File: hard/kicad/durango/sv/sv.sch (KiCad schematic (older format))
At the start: 27 parts, among them J1 6502 DATA BUS, J2 SVGA, J3 CONTROL, J4 6502 ADDRESS BUS, U1 74HCT02, U10 74HC245, U11 74HCT374, U12 74HC245, U13 74HC257, U14 6264, U15 74HC257, U16 74HC257, U17 74HC257, U18 74HC257, U2 74HCT4040, U3 74HC21, U4 74HCT4040, U5 74HC21, U6 74HCT85, U7 74HCT85, U8 74HCT85, U9 74HC175, X1 ACO-18.432MHz

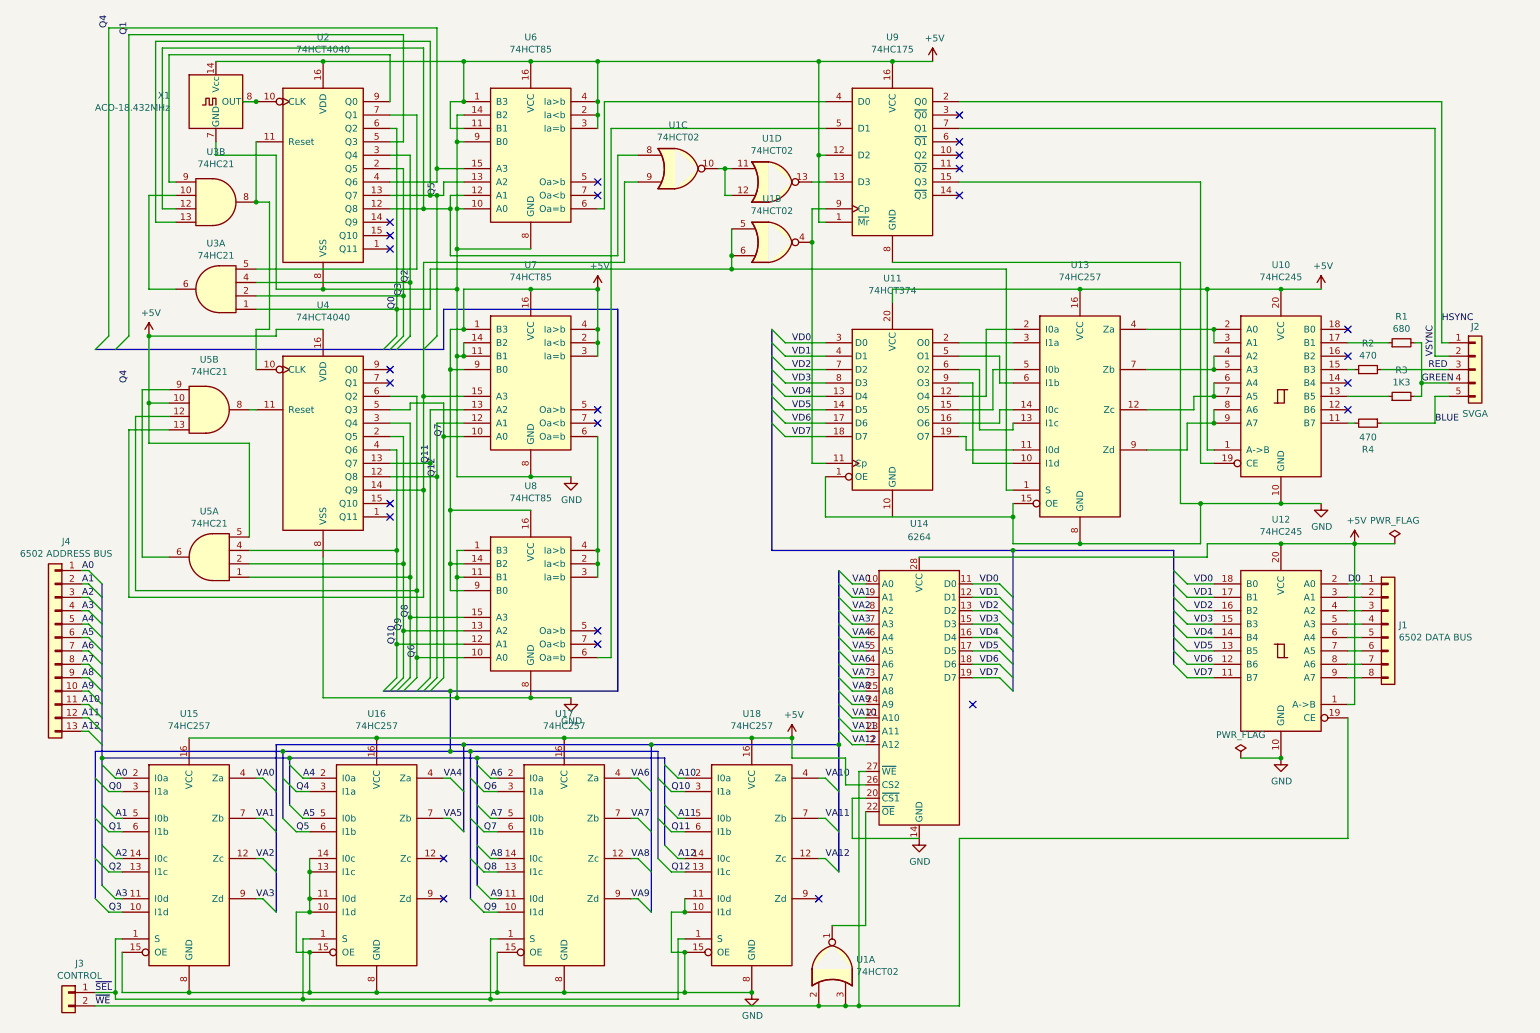
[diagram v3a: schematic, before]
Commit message: line clock from HS on all tree VDUs
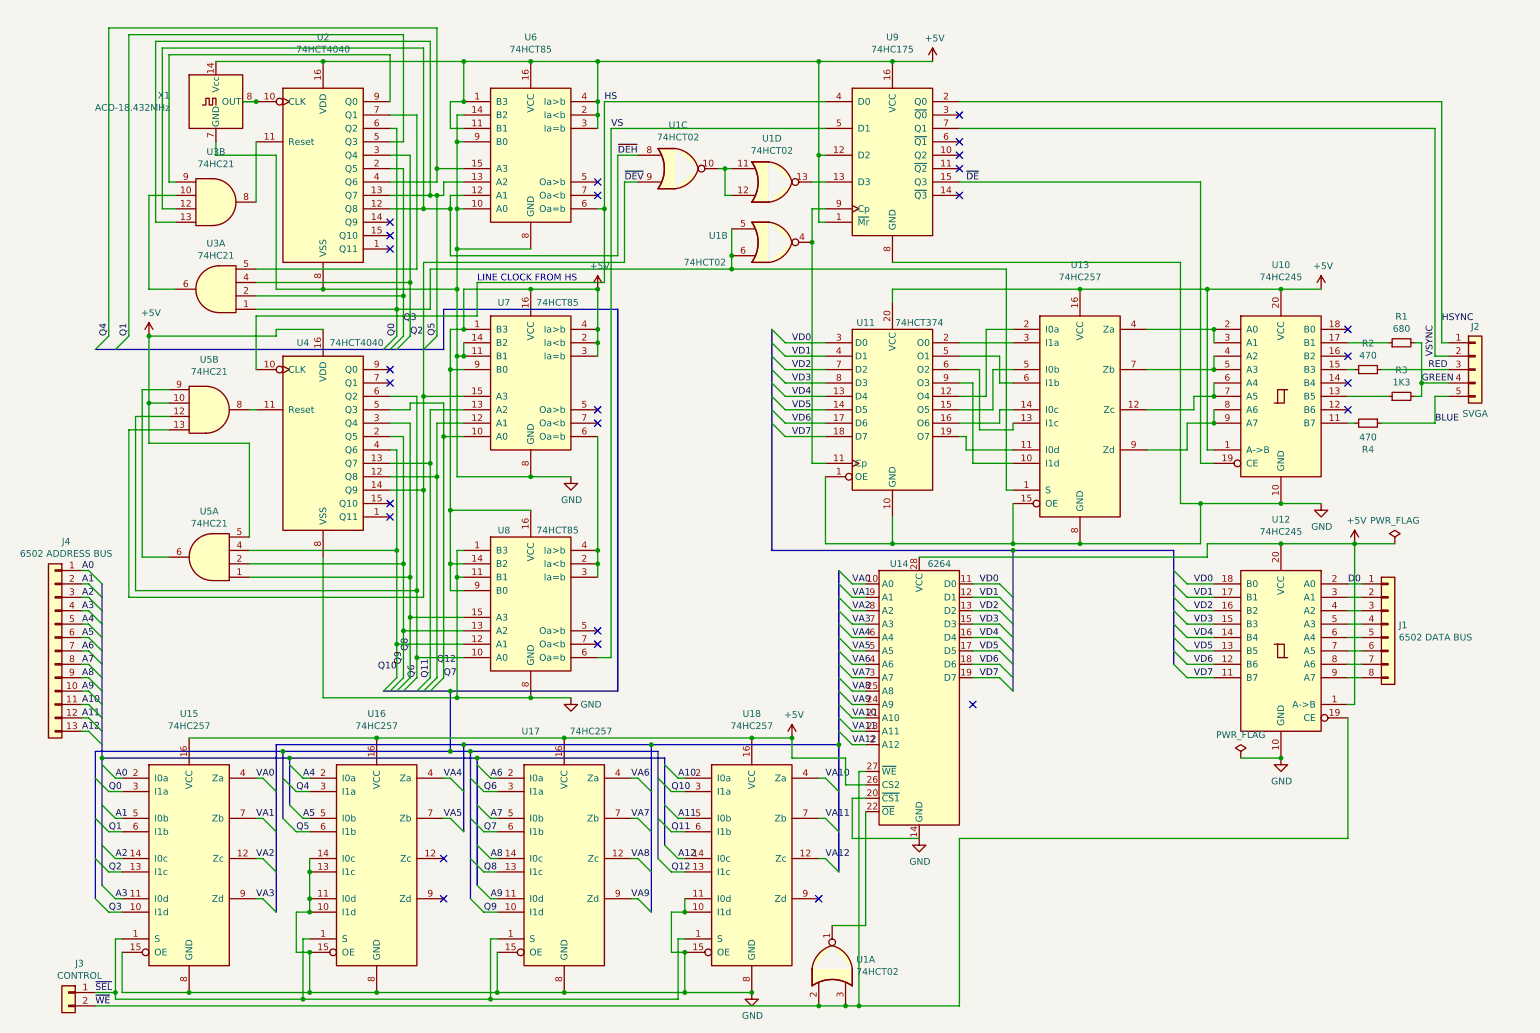
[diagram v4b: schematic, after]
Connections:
- net GND: now also U11.10 (GND)
- net ~DEH: now reaches U1.8, U2.12 (Q8), U3.12, U6.12 (A1)
- net ~DEV: now reaches U1.9, U4.14 (Q9), U5.13, U7.15 (A3)
- net at U2.11 (Reset), U3.8: no longer U4.10 (CLK)
- net HS: now reaches U6.6 (Oa=b), U9.4 (D0)
- net HS: now also U4.10 (CLK)
- net VS: now reaches U8.6 (Oa=b), U9.5 (D1)
- net ~DE: now reaches U10.19 (CE), U9.15 (Q3)
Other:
- note added: "LINE CLOCK FROM HS"
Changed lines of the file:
@@
 EESchema Schematic File Version 4
-LIBS:sv-cache
-EELAYER 29 0
+EELAYER 30 0
 EELAYER END
 $Descr A4 11693 8268
@@
 U 1 1 6066AB07
 P 2400 3500
-F 0 "U4" H 2400 4481 50  0000 C CNN
-F 1 "74HCT4040" H 2400 4390 50  0000 C CNN
+F 0 "U4" H 2250 4200 50  0000 C CNN
+F 1 "74HCT4040" H 2650 4200 50  0000 C CNN
 F 2 "" H 2400 3500 50  0001 C CNN
 F 3 "http://www.intersil.com/content/dam/Intersil/documents/cd40/cd4020bms-24bms-40bms.pdf" H 2400 3500 50  0001 C CNN
@@
 U 1 1 60692E60
 P 3950 3100
-F 0 "U7" H 3950 3981 50  0000 C CNN
-F 1 "74HCT85" H 3950 3890 50  0000 C CNN
+F 0 "U7" H 3750 3700 50  0000 C CNN
+F 1 "74HCT85" H 4150 3700 50  0000 C CNN
 F 2 "" H 3950 3100 50  0001 C CNN
 F 3 "http://www.ti.com/lit/gpn/sn74LS85" H 3950 3100 50  0001 C CNN
@@
 U 1 1 6069676C
 P 3950 4750
-F 0 "U8" H 3950 5631 50  0000 C CNN
-F 1 "74HCT85" H 3950 5540 50  0000 C CNN
+F 0 "U8" H 3750 5300 50  0000 C CNN
+F 1 "74HCT85" H 4150 5300 50  0000 C CNN
 F 2 "" H 3950 4750 50  0001 C CNN
 F 3 "http://www.ti.com/lit/gpn/sn74LS85" H 3950 4750 50  0001 C CNN
@@
 U 1 1 6075F5C4
 P 6650 3300
-F 0 "U11" H 6650 4281 50  0000 C CNN
-F 1 "74HCT374" H 6650 4190 50  0000 C CNN
+F 0 "U11" H 6450 3950 50  0000 C CNN
+F 1 "74HCT374" H 6850 3950 50  0000 C CNN
 F 2 "" H 6650 3300 50  0001 C CNN
 F 3 "https://www.ti.com/lit/ds/symlink/cd74hct374.pdf" H 6650 3300 50  0001 C CNN
@@
 	1050 3150 1250 3150
 Wire Wire Line
-	1900 1750 2000 1750
-Wire Wire Line
-	2000 1750 2000 2700
-Wire Wire Line
-	2000 2700 1900 2700
-Wire Wire Line
-	1900 2700 1900 3000
-Connection ~ 1900 1750
-Wire Wire Line
 	1900 2550 2950 2550
 Wire Wire Line
@@
 Connection ~ 9050 3400
 Wire Wire Line
-	7550 4000 7550 4100
-Wire Wire Line
 	7550 4300 8050 4300
 Wire Wire Line
@@
 U 2 1 60C66774
 P 5750 2050
-F 0 "U1" H 5750 2375 50  0000 C CNN
-F 1 "74HCT02" H 5750 2284 50  0000 C CNN
+F 0 "U1" H 5350 2100 50  0000 C CNN
+F 1 "74HCT02" H 5250 1900 50  0000 C CNN
 F 2 "" H 5750 2050 50  0001 C CNN
 F 3 "http://www.ti.com/lit/gpn/sn7402" H 5750 2050 50  0001 C CNN
@@
 P 4250 5450
 F 0 "#PWR0107" H 4250 5200 50  0001 C CNN
-F 1 "GND" H 4255 5277 50  0000 C CNN
+F 1 "GND" H 4400 5400 50  0000 C CNN
 F 2 "" H 4250 5450 50  0001 C CNN
 F 3 "" H 4250 5450 50  0001 C CNN
@@
 	1600 1400 1600 1300
 Connection ~ 2400 2400
-Connection ~ 7550 4100
-Wire Wire Line
-	7550 4100 7550 4300
 Wire Wire Line
 	8050 4300 8950 4300
@@
 U 1 1 606818EE
 P 6850 5400
-F 0 "U14" H 6850 6650 50  0000 C CNN
-F 1 "6264" H 6850 6550 50  0000 C CNN
+F 0 "U14" H 6700 6350 50  0000 C CNN
+F 1 "6264" H 7000 6350 50  0000 C CNN
 F 2 "Package_DIP:DIP-28_W15.24mm" H 6850 5400 50  0001 C CNN
 F 3 "http://users.ece.utexas.edu/~valvano/Datasheets/MCM6264.pdf" H 6850 5400 50  0001 C CNN
@@
 U 1 1 608343C4
 P 4200 6650
-F 0 "U17" H 4200 7731 50  0000 C CNN
-F 1 "74HC257" H 4200 7640 50  0000 C CNN
+F 0 "U17" H 3950 7600 50  0000 C CNN
+F 1 "74HC257" H 4400 7600 50  0000 C CNN
 F 2 "" H 4200 6650 50  0001 C CNN
 F 3 "http://www.ti.com/lit/gpn/sn74LS257" H 4200 6650 50  0001 C CNN
@@
 	3250 3800 3250 5300
 Connection ~ 3250 3800
-Text Label 3250 3800 1    50   ~ 0
+Text Label 3250 5200 0    50   ~ 0
 Q12
 Wire Wire Line
 	3300 3500 3300 5300
 Connection ~ 3300 3500
-Text Label 3300 3500 1    50   ~ 0
+Text Label 3300 5300 0    50   ~ 0
 Q7
 Wire Wire Line
 	3200 3700 3200 5300
 Connection ~ 3200 3700
-Text Label 3200 3700 1    50   ~ 0
+Text Label 3200 5300 1    50   ~ 0
 Q11
 Wire Wire Line
 	2950 5050 2950 5300
 Connection ~ 2950 5050
-Text Label 2950 5050 1    50   ~ 0
+Text Label 2950 5250 2    50   ~ 0
 Q10
 Wire Wire Line
 	3000 4950 3000 5300
 Connection ~ 3000 4950
-Text Label 3000 4950 1    50   ~ 0
+Text Label 3000 5200 1    50   ~ 0
 Q9
 Wire Wire Line
 	3050 4850 3050 5300
 Connection ~ 3050 4850
-Text Label 3050 4850 1    50   ~ 0
+Text Label 3050 5100 1    50   ~ 0
 Q8
 Wire Wire Line
 	3100 5150 3100 5300
 Connection ~ 3100 5150
-Text Label 3100 5150 1    50   ~ 0
+Text Label 3100 5300 1    50   ~ 0
 Q6
 Entry Wire Line
@@
 Wire Wire Line
 	2950 2550 2950 2750
-Text Label 2950 2550 1    50   ~ 0
+Text Label 2950 2750 1    50   ~ 0
 Q0
 Wire Wire Line
 	3050 2350 3050 2750
 Connection ~ 3050 2350
-Text Label 3050 2350 1    50   ~ 0
+Text Label 3050 2750 0    50   ~ 0
 Q2
 Wire Wire Line
 	3000 2450 3000 2750
 Connection ~ 3000 2450
-Text Label 3000 2450 1    50   ~ 0
+Text Label 3000 2650 0    50   ~ 0
 Q3
 Wire Wire Line
@@
 Wire Wire Line
 	3250 1700 3300 1700
-Text Label 3250 1700 1    50   ~ 0
+Text Label 3250 2650 3    50   ~ 0
 Q5
 Wire Wire Line
@@
 Wire Wire Line
 	950  500  950  2750
-Text Label 950  500  1    50   ~ 0
+Text Label 950  2750 1    50   ~ 0
 Q1
 Wire Wire Line
@@
 Wire Wire Line
 	800  450  800  2750
-Text Label 950  3100 1    50   ~ 0
-Q4
 Entry Wire Line
 	700  2850 800  2750
@@
 	2150 5900 750  5900
 Connection ~ 2150 5900
-Text Label 800  450  1    50   ~ 0
+Text Label 800  2750 1    50   ~ 0
 Q4
 Wire Wire Line
@@
 	850  7700 2250 7700
 NoConn ~ 7250 5500
-Wire Wire Line
-	6150 3800 6150 4100
 $Comp
 L Connector_Generic:Conn_01x08 J1
@@
 Connection ~ 6400 7750
 Wire Wire Line
-	6150 4100 7550 4100
+	1900 2600 1900 3000
+Wire Wire Line
+	1900 2600 3550 2600
+Wire Wire Line
+	3550 2600 3550 2350
+Wire Wire Line
+	3550 2350 4500 2350
+Wire Wire Line
+	4500 2350 4500 1800
+Connection ~ 4500 1800
+Text Notes 3550 2350 0    50   ~ 0
+LINE CLOCK FROM HS
+Text Label 4500 1000 0    50   ~ 0
+HS
+Text Label 4550 1200 0    50   ~ 0
+VS
+Text Label 7200 1600 0    50   ~ 0
+~DE
+Text Label 4600 1400 0    50   ~ 0
+~DEH
+Text Label 4650 1600 0    50   ~ 0
+~DEV
+Wire Wire Line
+	7550 4000 7550 4300
+Wire Wire Line
+	6150 3800 6150 4300
+Wire Wire Line
+	6150 4300 6650 4300
+Connection ~ 7550 4300
+Wire Wire Line
+	6650 4100 6650 4300
 Wire Wire Line
 	3150 2200 3150 3200
@@
 Wire Bus Line
 	750  4600 750  5900
+Connection ~ 6650 4300
+Wire Wire Line
+	6650 4300 7550 4300
 $EndSCHEMATC
